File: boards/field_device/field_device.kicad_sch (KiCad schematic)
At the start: 0 parts

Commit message: RF fun is soon!
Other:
- added sheet lora_module (lora_module.kicad_sch)
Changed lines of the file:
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@@
+	)
+	(sheet
+		(at 85.09 59.69)
+		(size 20.32 11.43)
+		(exclude_from_sim no)
+		(in_bom yes)
+		(on_board yes)
+		(dnp no)
+		(fields_autoplaced yes)
+		(stroke
+			(width 0.1524)
+			(type solid)
+		)
+		(fill
+			(color 0 0 0 0)
+		)
+		(property "Sheetname" "lora_module"
+			(at 85.09 58.9784 0)
+			(show_name no)
+			(do_not_autoplace no)
+			(effects
+				(font
+					(size 1.27 1.27)
+				)
+				(justify left bottom)
+			)
+		)
+		(property "Sheetfile" "lora_module.kicad_sch"
+			(at 85.09 71.7046 0)
+			(show_name no)
+			(do_not_autoplace no)
+			(effects
+				(font
+					(size 1.27 1.27)
+				)
+				(justify left top)
+			)
+		)
+		(instances
+			(project "field_device"
+				(path "/99623870-118f-49fe-bbf0-fb0b890db442"
+					(page "7")
+				)
+			)
+		)
 	)
 	(sheet

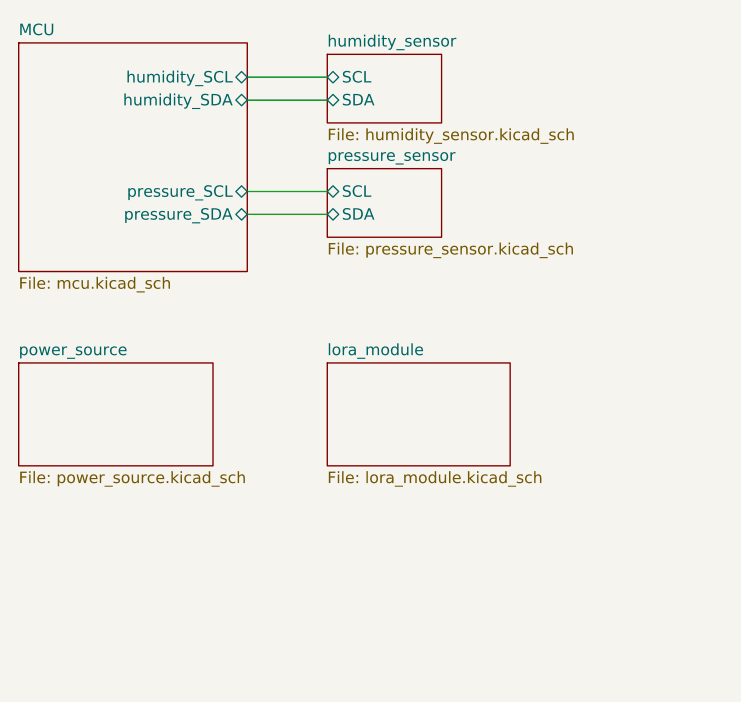
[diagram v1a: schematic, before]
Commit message: connected lora to mcu
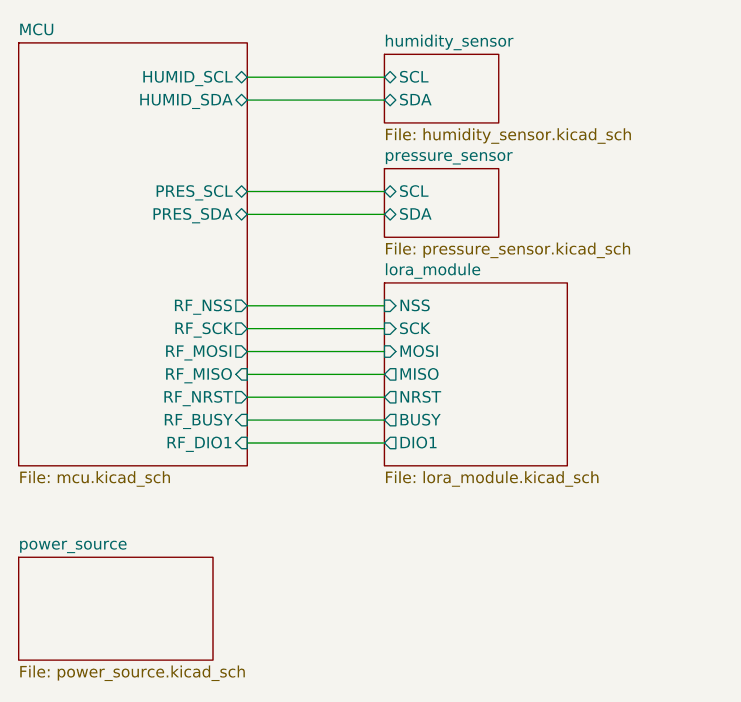
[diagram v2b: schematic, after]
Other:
- sheet MCU ports: added HUMID_SCL, HUMID_SDA, PRES_SCL, PRES_SDA, RF_BUSY, RF_DIO1, RF_MISO, RF_MOSI, RF_NRST, RF_NSS, RF_SCK; removed humidity_SCL, humidity_SDA, pressure_SCL, pressure_SDA
- sheet lora_module ports: added BUSY, DIO1, MISO, MOSI, NRST, NSS, SCK; removed none

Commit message: rev 5?
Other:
- title: (none) -> Field Device
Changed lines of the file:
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@@
 	(generator_version "10.0")
 	(paper "A4")
+	(title_block
+		(title "Field Device")
+		(date "2026-10-09")
+		(rev "5")
+	)
 	(wire
 		(pts
